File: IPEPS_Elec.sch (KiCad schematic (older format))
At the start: 47 parts

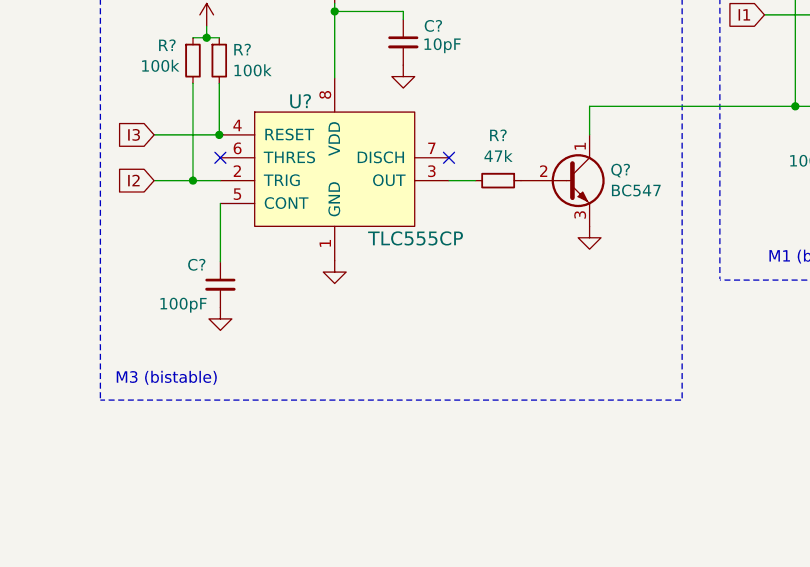
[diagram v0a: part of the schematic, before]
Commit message: merge M3 GND points
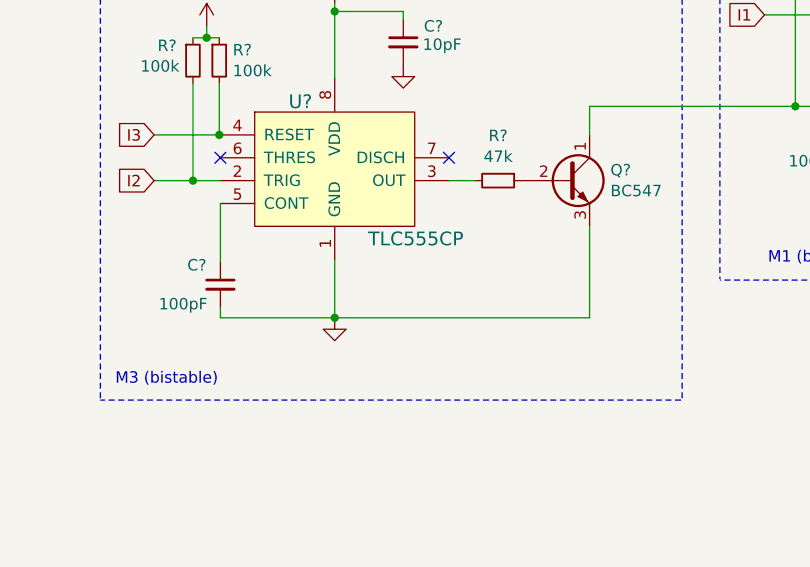
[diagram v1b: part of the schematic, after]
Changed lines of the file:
@@
-$Comp
-L power:GND #PWR?
-U 1 1 6193A4A7
-P 3725 3075
-F 0 "#PWR?" H 3725 2825 50  0001 C CNN
-F 1 "GND" H 3730 2902 50  0001 C CNN
-F 2 "" H 3725 3075 50  0001 C CNN
-F 3 "" H 3725 3075 50  0001 C CNN
-	1    3725 3075
-	1    0    0    -1
-$EndComp
 $Comp
 L power:GND #PWR?
@@
 	1    4440 2725
 	0    1    1    0
-$EndComp
-$Comp
-L power:GND #PWR?
-U 1 1 619BA743
-P 4840 2925
-F 0 "#PWR?" H 4840 2675 50  0001 C CNN
-F 1 "GND" H 4845 2752 50  0001 C CNN
-F 2 "" H 4840 2925 50  0001 C CNN
-F 3 "" H 4840 2925 50  0001 C CNN
-	1    4840 2925
-	1    0    0    -1
 $EndComp
 Wire Wire Line
@@
 L power:GND #PWR?
 U 1 1 6195DC61
-P 3225 3280
-F 0 "#PWR?" H 3225 3030 50  0001 C CNN
-F 1 "GND" H 3230 3107 50  0001 C CNN
-F 2 "" H 3225 3280 50  0001 C CNN
-F 3 "" H 3225 3280 50  0001 C CNN
-	1    3225 3280
+P 3725 3325
+F 0 "#PWR?" H 3725 3075 50  0001 C CNN
+F 1 "GND" H 3730 3152 50  0001 C CNN
+F 2 "" H 3725 3325 50  0001 C CNN
+F 3 "" H 3725 3325 50  0001 C CNN
+	1    3725 3325
 	1    0    0    -1
 $EndComp
@@
 Wire Notes Line
 	1015 2095 1015 3735
+Wire Wire Line
+	3725 3075 3725 3325
+Wire Wire Line
+	3725 3325 3225 3325
+Wire Wire Line
+	3225 3280 3225 3325
+Wire Wire Line
+	4840 2925 4840 3325
+Wire Wire Line
+	4840 3325 3725 3325
+Connection ~ 3725 3325
 $EndSCHEMATC

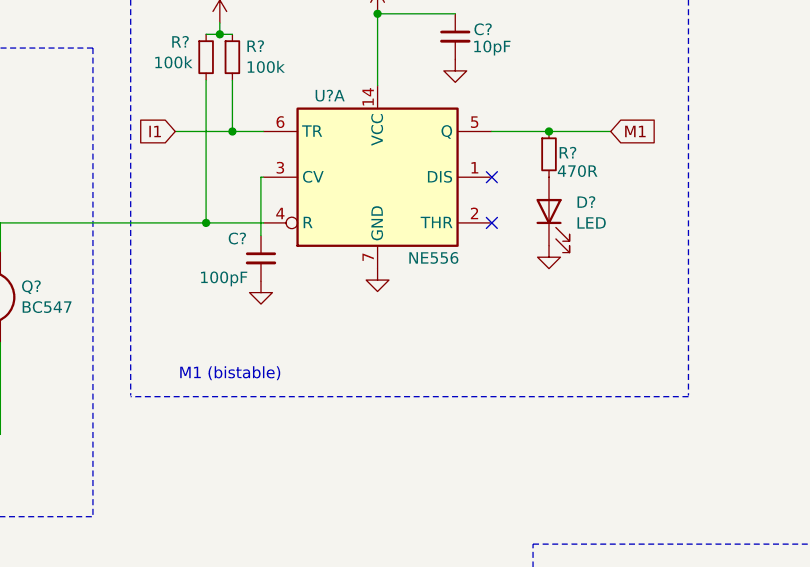
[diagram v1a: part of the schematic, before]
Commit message: merge M1 GND points
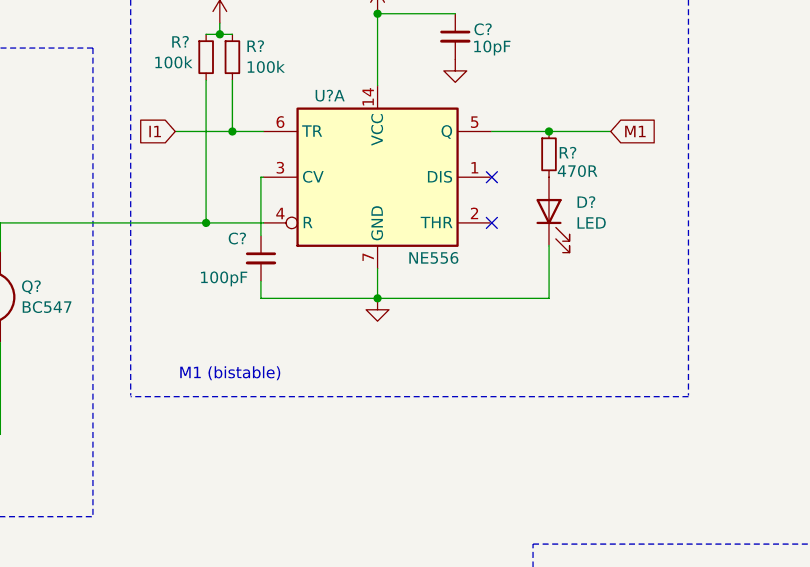
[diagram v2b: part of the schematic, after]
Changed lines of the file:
@@
-$Comp
-L power:GND #PWR?
-U 1 1 6192D39A
-P 6490 2600
-F 0 "#PWR?" H 6490 2350 50  0001 C CNN
-F 1 "GND" H 6495 2427 50  0001 C CNN
-F 2 "" H 6490 2600 50  0001 C CNN
-F 3 "" H 6490 2600 50  0001 C CNN
-	1    6490 2600
-	1    0    0    -1
-$EndComp
 $Comp
 L power:GND #PWR?
@@
 L power:GND #PWR?
 U 1 1 6194269E
-P 5980 2655
-F 0 "#PWR?" H 5980 2405 50  0001 C CNN
-F 1 "GND" H 5985 2482 50  0001 C CNN
-F 2 "" H 5980 2655 50  0001 C CNN
-F 3 "" H 5980 2655 50  0001 C CNN
-	1    5980 2655
+P 6490 2730
+F 0 "#PWR?" H 6490 2480 50  0001 C CNN
+F 1 "GND" H 6495 2557 50  0001 C CNN
+F 2 "" H 6490 2730 50  0001 C CNN
+F 3 "" H 6490 2730 50  0001 C CNN
+	1    6490 2730
 	1    0    0    -1
 $EndComp
@@
 	1    10310 2240
 	0    -1   -1   0
-$EndComp
-$Comp
-L power:GND #PWR?
-U 1 1 61A41B46
-P 7240 2500
-F 0 "#PWR?" H 7240 2250 50  0001 C CNN
-F 1 "GND" H 7245 2327 50  0001 C CNN
-F 2 "" H 7240 2500 50  0001 C CNN
-F 3 "" H 7240 2500 50  0001 C CNN
-	1    7240 2500
-	1    0    0    -1
 $EndComp
 $Comp
@@
 	4840 3325 3725 3325
 Connection ~ 3725 3325
+Wire Wire Line
+	5980 2655 5980 2730
+Wire Wire Line
+	5980 2730 6490 2730
+Wire Wire Line
+	7240 2730 7240 2500
+Wire Wire Line
+	6490 2600 6490 2730
+Connection ~ 6490 2730
+Wire Wire Line
+	6490 2730 7240 2730
 $EndSCHEMATC

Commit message: merge M2 GND points
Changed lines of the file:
@@
-$EndComp
-$Comp
-L power:GND #PWR?
-U 1 1 6192EC57
-P 9615 2440
-F 0 "#PWR?" H 9615 2190 50  0001 C CNN
-F 1 "GND" H 9620 2267 50  0001 C CNN
-F 2 "" H 9615 2440 50  0001 C CNN
-F 3 "" H 9615 2440 50  0001 C CNN
-	1    9615 2440
-	1    0    0    -1
 $EndComp
 $Comp
@@
 L power:GND #PWR?
 U 1 1 6196B3BE
-P 9105 2495
-F 0 "#PWR?" H 9105 2245 50  0001 C CNN
-F 1 "GND" H 9110 2322 50  0001 C CNN
-F 2 "" H 9105 2495 50  0001 C CNN
-F 3 "" H 9105 2495 50  0001 C CNN
-	1    9105 2495
+P 9615 2575
+F 0 "#PWR?" H 9615 2325 50  0001 C CNN
+F 1 "GND" H 9620 2402 50  0001 C CNN
+F 2 "" H 9615 2575 50  0001 C CNN
+F 3 "" H 9615 2575 50  0001 C CNN
+	1    9615 2575
 	1    0    0    -1
 $EndComp
@@
 	1    10310 2240
 	0    -1   -1   0
-$EndComp
-$Comp
-L power:GND #PWR?
-U 1 1 61A43982
-P 10310 2390
-F 0 "#PWR?" H 10310 2140 50  0001 C CNN
-F 1 "GND" H 10315 2217 50  0001 C CNN
-F 2 "" H 10310 2390 50  0001 C CNN
-F 3 "" H 10310 2390 50  0001 C CNN
-	1    10310 2390
-	1    0    0    -1
 $EndComp
 Text GLabel 8630 4200 1    50   Input ~ 0
@@
 Wire Wire Line
 	6490 2730 7240 2730
+Wire Wire Line
+	9105 2495 9105 2575
+Wire Wire Line
+	9105 2575 9615 2575
+Wire Wire Line
+	10310 2575 10310 2390
+Wire Wire Line
+	9615 2440 9615 2575
+Connection ~ 9615 2575
+Wire Wire Line
+	9615 2575 10310 2575
 $EndSCHEMATC

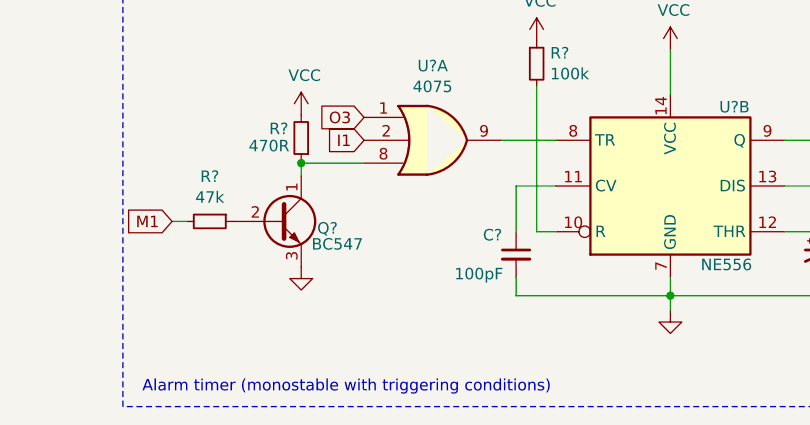
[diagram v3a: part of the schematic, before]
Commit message: merge alarm GND points
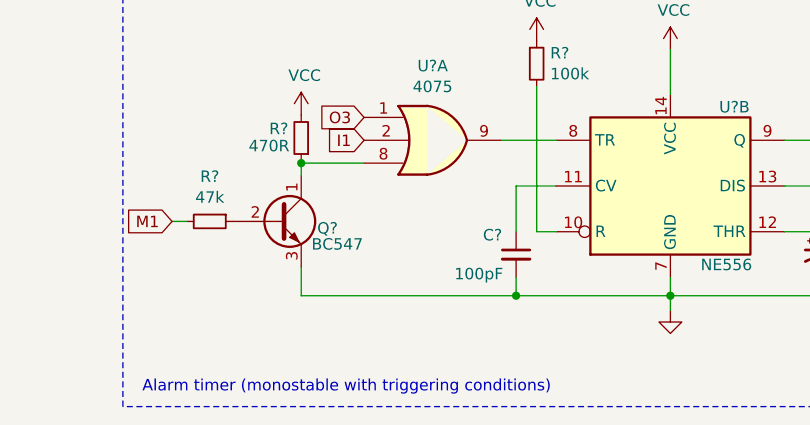
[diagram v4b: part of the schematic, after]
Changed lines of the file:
@@
 O3
-$Comp
-L power:GND #PWR?
-U 1 1 61A52278
-P 2875 6325
-F 0 "#PWR?" H 2875 6075 50  0001 C CNN
-F 1 "GND" H 2875 6185 50  0001 C CNN
-F 2 "" H 2875 6325 50  0001 C CNN
-F 3 "" H 2875 6325 50  0001 C CNN
-	1    2875 6325
-	1    0    0    -1
-$EndComp
 $Comp
 L power:VCC #PWR?
@@
 Wire Wire Line
 	9615 2575 10310 2575
+Wire Wire Line
+	2875 6325 2875 6450
+Wire Wire Line
+	2875 6450 3815 6450
+Connection ~ 3815 6450
 $EndSCHEMATC

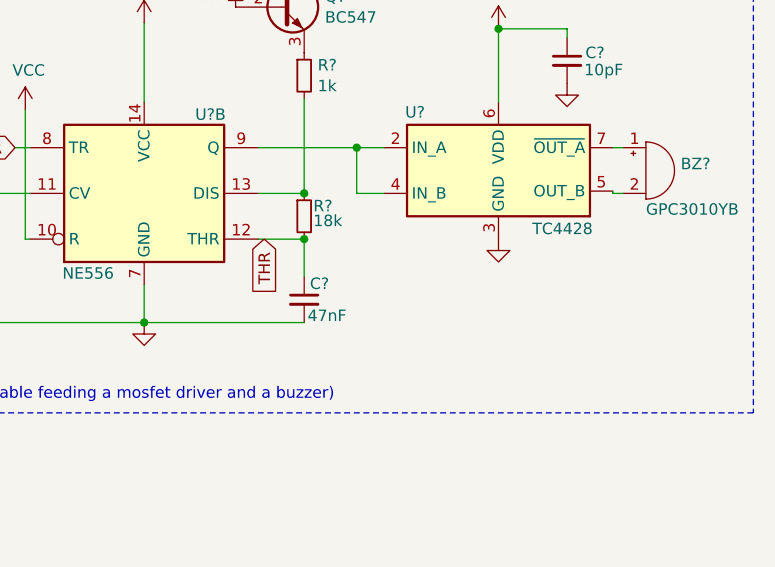
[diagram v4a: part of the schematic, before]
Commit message: merge alarm GND points
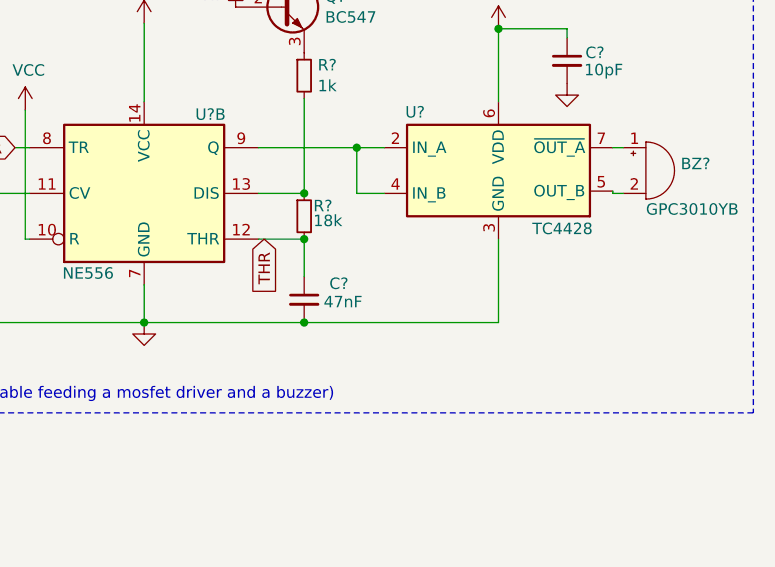
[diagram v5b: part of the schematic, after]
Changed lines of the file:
@@
 	10280 5215 10325 5215
-$Comp
-L power:GND #PWR?
-U 1 1 61A13BDD
-P 9780 5415
-F 0 "#PWR?" H 9780 5165 50  0001 C CNN
-F 1 "GND" H 9785 5242 50  0001 C CNN
-F 2 "" H 9780 5415 50  0001 C CNN
-F 3 "" H 9780 5415 50  0001 C CNN
-	1    9780 5415
-	1    0    0    -1
-$EndComp
 $Comp
 L power:VCC #PWR?
@@
 U 1 1 619A543A
 P 8930 5680
-F 0 "C?" H 8955 5750 50  0000 L CNN
-F 1 "47nF" H 8945 5610 50  0000 L CNN
+F 0 "C?" H 9040 5750 50  0000 L CNN
+F 1 "47nF" H 9015 5670 50  0000 L CNN
 F 2 "" H 8930 5680 50  0001 C CNN
 F 3 "~" H 8930 5680 50  0001 C CNN
@@
 	2875 6450 3815 6450
 Connection ~ 3815 6450
+Wire Wire Line
+	9780 5415 9780 5780
+Wire Wire Line
+	9780 5780 8930 5780
+Connection ~ 8930 5780
 $EndSCHEMATC

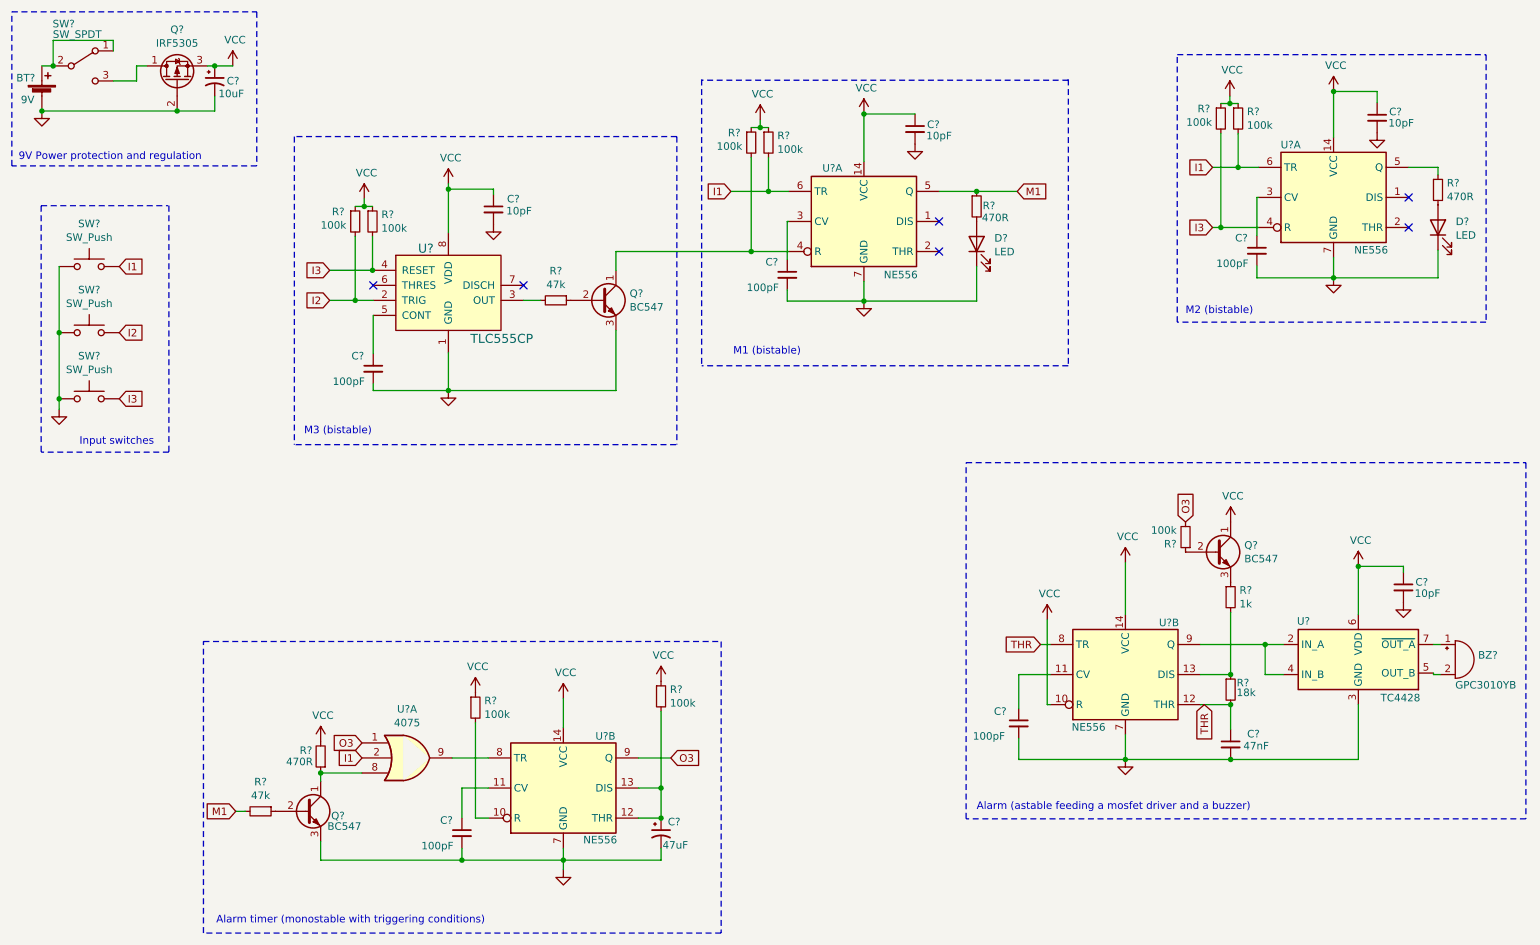
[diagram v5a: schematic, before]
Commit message: change decoupling capacitors values
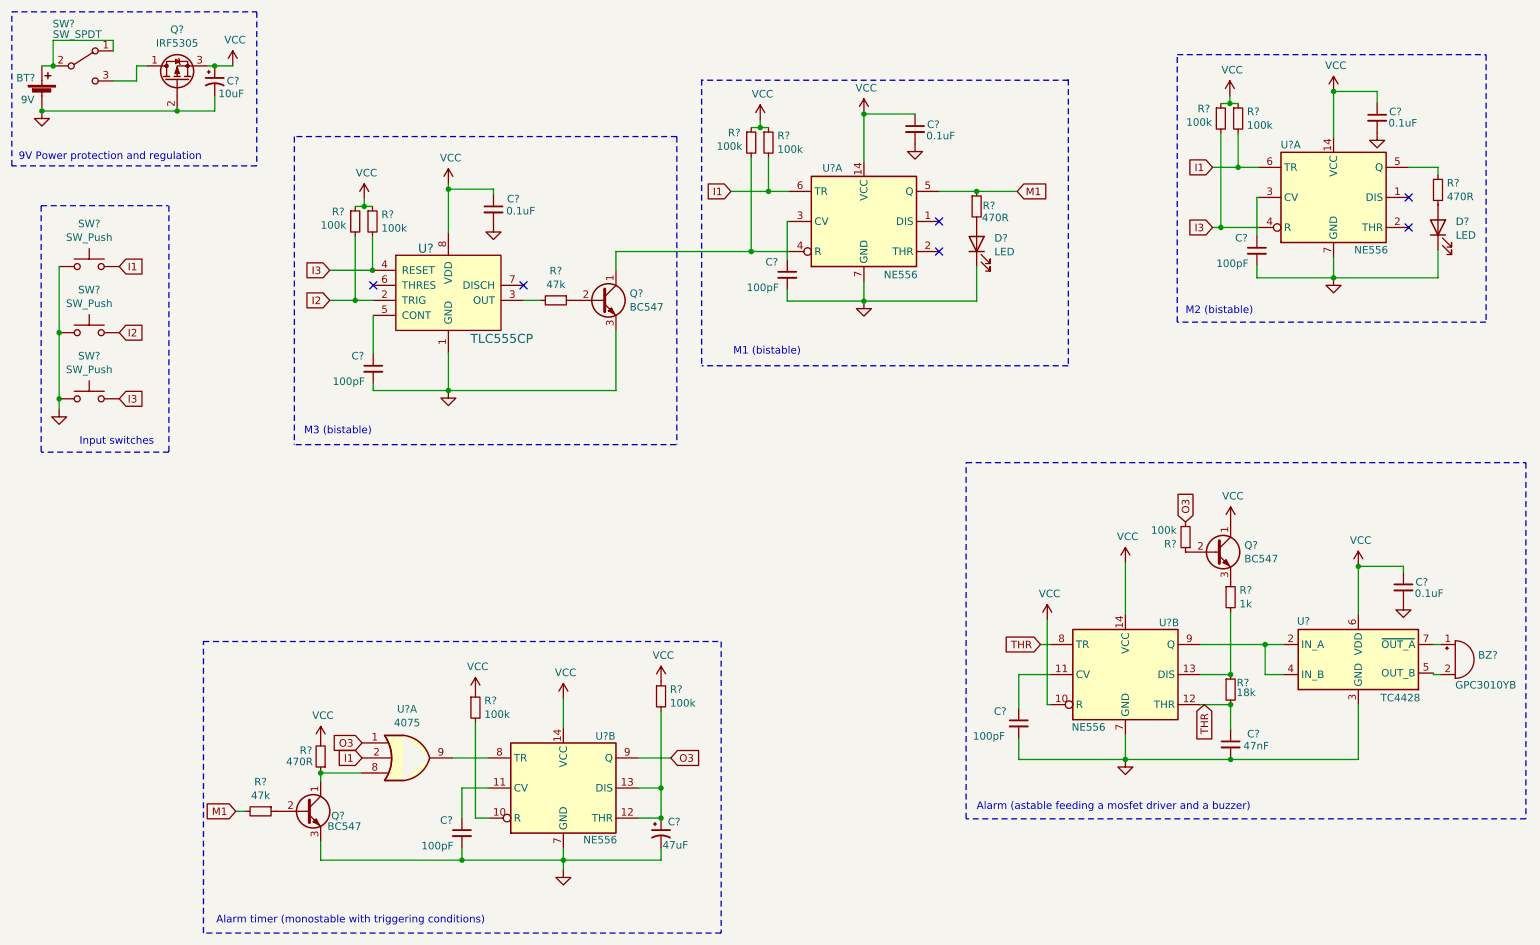
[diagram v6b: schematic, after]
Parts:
- C? (x4): value 10pF -> 0.1uF
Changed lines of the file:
@@
 P 4025 2120
 F 0 "C?" H 4115 2190 50  0000 L CNN
-F 1 "10pF" H 4110 2110 50  0000 L CNN
+F 1 "0.1uF" H 4110 2110 50  0000 L CNN
 F 2 "" H 4025 2120 50  0001 C CNN
 F 3 "~" H 4025 2120 50  0001 C CNN
@@
 P 6830 1585
 F 0 "C?" H 6910 1615 50  0000 L CNN
-F 1 "10pF" H 6905 1540 50  0000 L CNN
+F 1 "0.1uF" H 6905 1540 50  0000 L CNN
 F 2 "" H 6830 1585 50  0001 C CNN
 F 3 "~" H 6830 1585 50  0001 C CNN
@@
 P 9905 1510
 F 0 "C?" H 9985 1550 50  0000 L CNN
-F 1 "10pF" H 9980 1475 50  0000 L CNN
+F 1 "0.1uF" H 9980 1475 50  0000 L CNN
 F 2 "" H 9905 1510 50  0001 C CNN
 F 3 "~" H 9905 1510 50  0001 C CNN
@@
 P 10080 4635
 F 0 "C?" H 10160 4670 50  0000 L CNN
-F 1 "10pF" H 10155 4595 50  0000 L CNN
+F 1 "0.1uF" H 10155 4595 50  0000 L CNN
 F 2 "" H 10080 4635 50  0001 C CNN
 F 3 "~" H 10080 4635 50  0001 C CNN

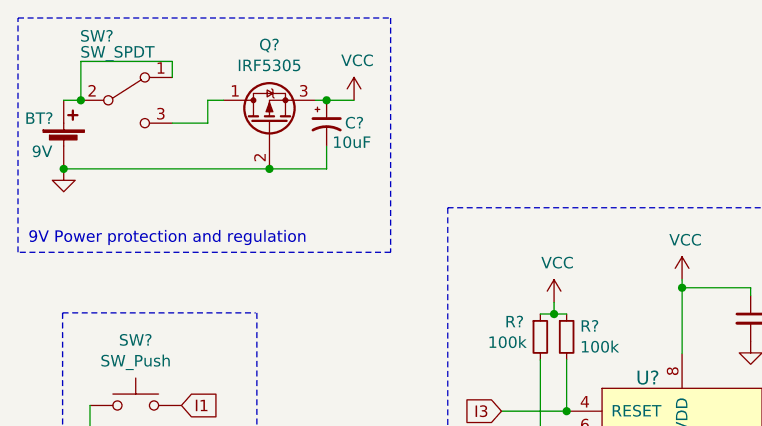
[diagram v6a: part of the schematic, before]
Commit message: change bulk decoupling capacitor
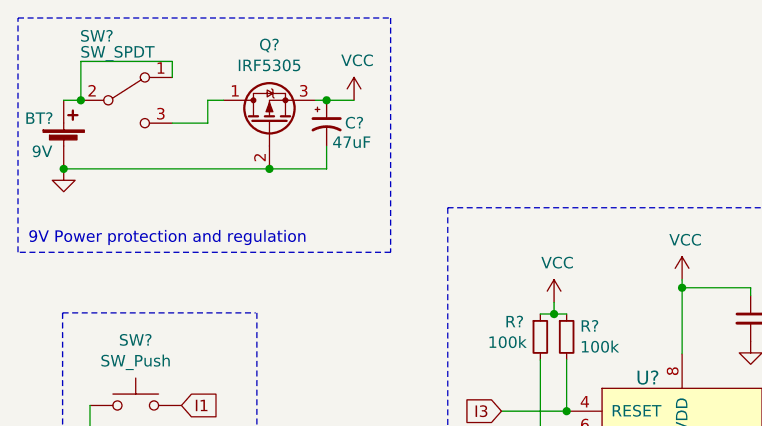
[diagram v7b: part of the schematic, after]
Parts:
- C?: value 10uF -> 47uF
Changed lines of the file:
@@
 P 2170 1265
 F 0 "C?" H 2250 1265 50  0000 L CNN
-F 1 "10uF" H 2195 1180 50  0000 L CNN
+F 1 "47uF" H 2195 1180 50  0000 L CNN
 F 2 "" H 2170 1265 50  0001 C CNN
 F 3 "~" H 2170 1265 50  0001 C CNN
